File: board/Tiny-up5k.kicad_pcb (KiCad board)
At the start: 2 copper layers, 17.8 x 35.6 mm, 37 parts, among them J1 CONN_01X14, J2 CONN_01X14, J5 Prog, SW1 SW_Push, U1 ICE40UP5K-SG48ITR, U2 MIC5504-3.3YM5, U3 DSC6001CI2A-016.0000T, U4 MIC5504-1.2YM5, U5 SST25VF016B, U6 USB_OTG

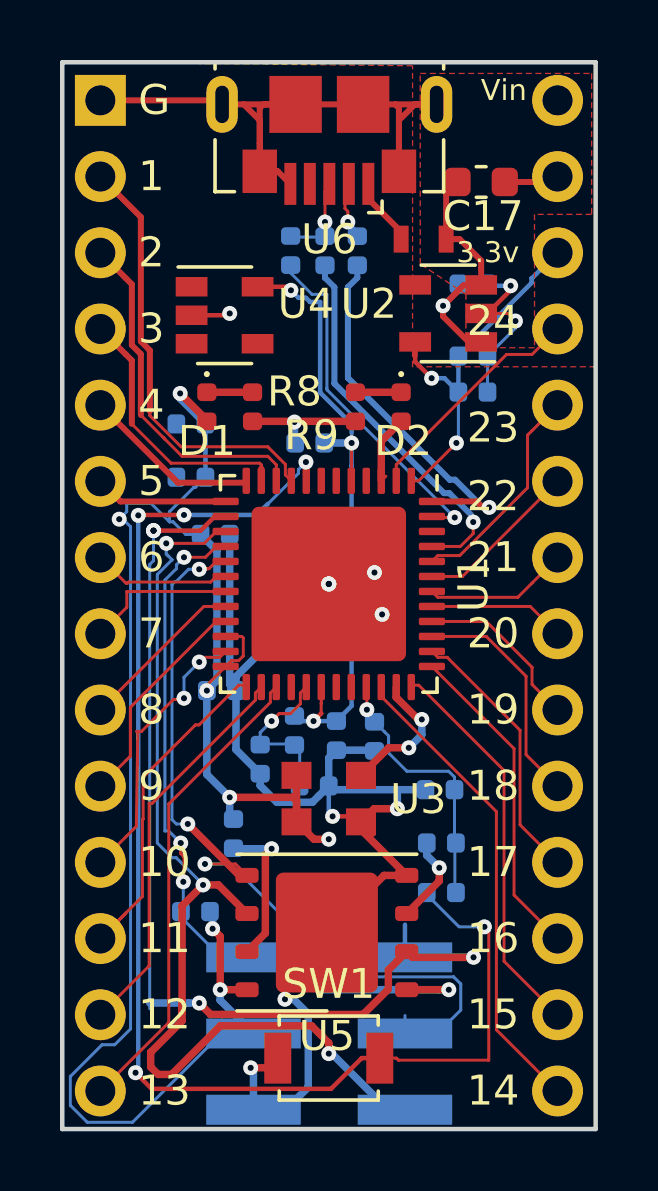
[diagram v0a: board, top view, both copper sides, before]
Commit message: Fix SPI line and send rev03 to aisler
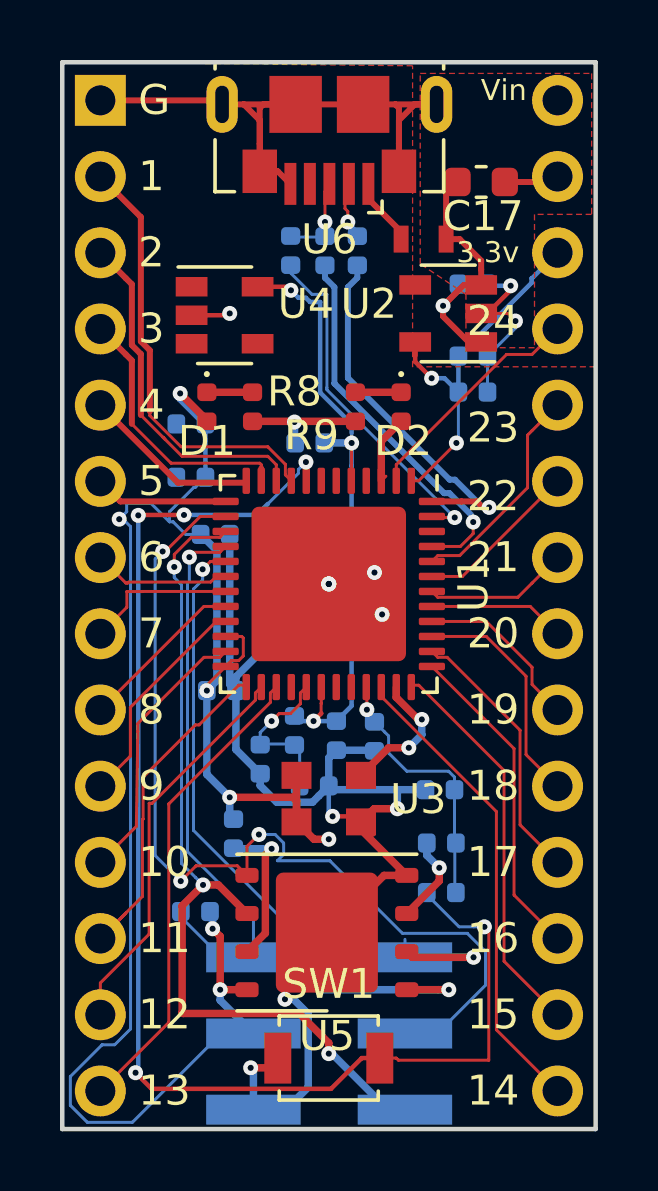
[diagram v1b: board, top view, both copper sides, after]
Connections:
- U1 pad 14: SDI -> SDO
- U1 pad 17: SDO -> SDI
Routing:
- net SDI: track 34.3 -> 24.1 mm, vias 4 -> 2
- net SCK: track 35.3 -> 30.3 mm
- net SDO: track 28.7 -> 33.1 mm
- net SS: track 25.5 -> 27.6 mm, vias 4 -> 2
- net HL_11: track 9.38 -> 9.05 mm, vias 2 -> 0
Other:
- board text added: "Tiny-up5k 0x03"
- board text removed: "Tiny-up5k"
